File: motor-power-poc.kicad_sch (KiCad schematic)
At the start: 47 parts, among them J5 Conn_01x04_Pin, SW1 SW_Push, SW2 SW_Push, U1 QRE1113GR, U2 QRE1113GR, U3 QRE1113GR, U4 ESP32-S3FH4R2, Y1 48M

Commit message: schem: add ordering info to BOM
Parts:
- C2, C3, C4: Basic (none) -> Y; JLCPCB Part # (none) -> C307331; Manufacturer (none) -> Samsung Electro-Mechanics; Manufacturer Part Number (none) -> CL05B104KB54PNC
- R1, R2, R3: footprint Resistor_SMD:R_0402_1005Metric -> Resistor_SMD:R_0603_1608Metric; Basic (none) -> Y; JLCPCB Part # (none) -> C23212; Manufacturer (none) -> Uniroyal Elec; Manufacturer Part Number (none) -> 0603WAF6801T5E
- R4: Basic (none) -> Y; JLCPCB Part # (none) -> C23182; Manufacturer (none) -> Uniroyal Elec; Manufacturer Part Number (none) -> 0603WAF470JT5E
- R5: Basic (none) -> Y; JLCPCB Part # (none) -> C4275; Manufacturer (none) -> Uniroyal Elec; Manufacturer Part Number (none) -> 0603WAF750JT5E
- R6: Basic (none) -> Y; JLCPCB Part # (none) -> C22775; Manufacturer (none) -> Uniroyal Elec; Manufacturer Part Number (none) -> 0603WAF1000T5E
- TP1: Basic (none) -> X; JLCPCB Part # (none) -> C2906768; Manufacturer (none) -> Keystone; Manufacturer Part Number (none) -> 5015
- U1, U2, U3: Basic (none) -> X; JLCPCB Part # (none) -> C232862; Manufacturer (none) -> onsemi; Manufacturer Part Number (none) -> QRE1113GR

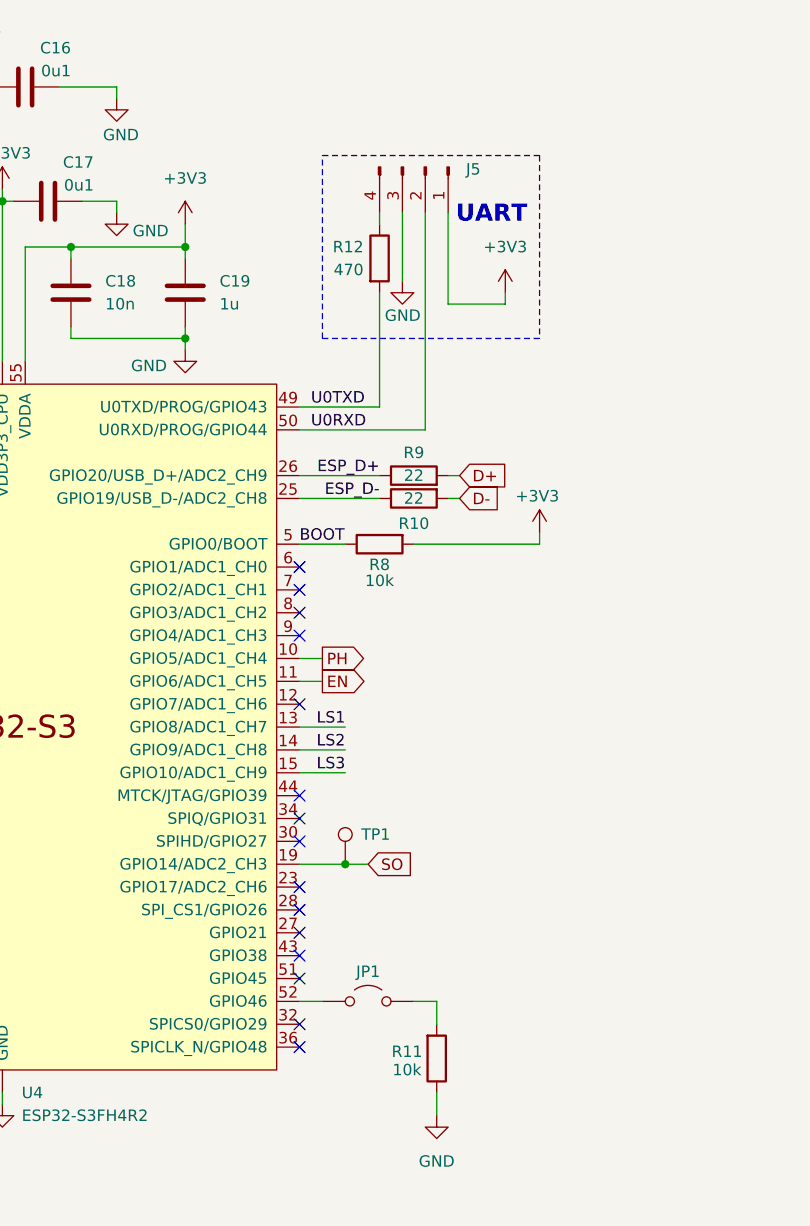
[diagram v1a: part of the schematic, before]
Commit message: schem: renumber
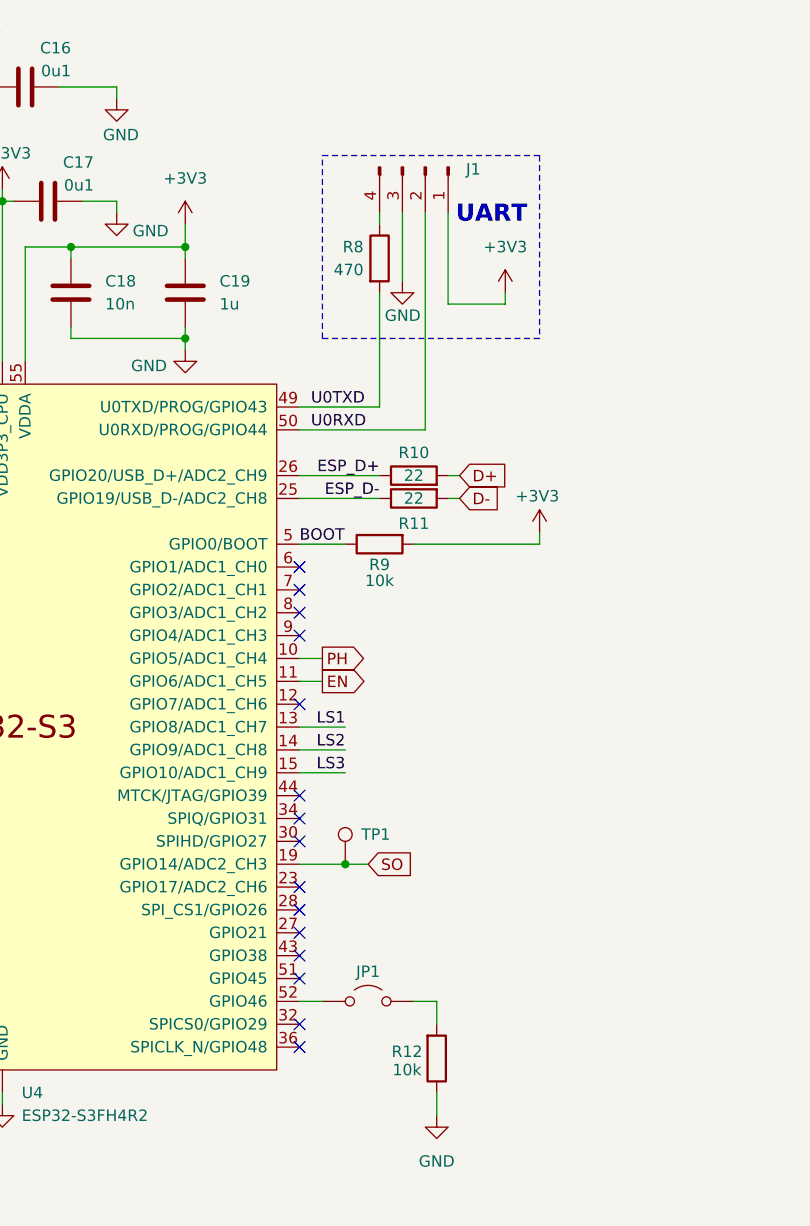
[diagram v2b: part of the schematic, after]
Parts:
- renumbered J5 to J1, R9 to R10, R10 to R11, R11 to R12, R12 to R8, R8 to R9
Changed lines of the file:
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@@
 		(on_board yes)
 		(dnp no)
-		(property "Reference" "R10"
+		(property "Reference" "R11"
 			(at 245.11 70.104 90)
 			(effects
@@
 			(project "motor-power-poc"
 				(path "/a1dc4c9e-7b20-4b66-a693-9133bc644c6b"
-					(reference "R10")
+					(reference "R11")
 					(unit 1)
 				)
@@
 		(on_board yes)
 		(dnp no)
-		(property "Reference" "J5"
+		(property "Reference" "J1"
 			(at 251.714 30.734 90)
 			(effects
@@
 			(project "motor-power-poc"
 				(path "/a1dc4c9e-7b20-4b66-a693-9133bc644c6b"
-					(reference "J5")
+					(reference "J1")
 					(unit 1)
 				)
@@
 		(dnp no)
 		(fields_autoplaced yes)
-		(property "Reference" "#PWR029"
+		(property "Reference" "#PWR030"
 			(at 247.65 142.24 0)
 			(effects
@@
 			(project "motor-power-poc"
 				(path "/a1dc4c9e-7b20-4b66-a693-9133bc644c6b"
-					(reference "#PWR029")
+					(reference "#PWR030")
 					(unit 1)
 				)
@@
 		(on_board yes)
 		(dnp no)
-		(property "Reference" "R9"
+		(property "Reference" "R10"
 			(at 245.11 62.23 90)
 			(effects
@@
 			(project "motor-power-poc"
 				(path "/a1dc4c9e-7b20-4b66-a693-9133bc644c6b"
-					(reference "R9")
+					(reference "R10")
 					(unit 1)
 				)
@@
 		(on_board yes)
 		(dnp no)
-		(property "Reference" "R11"
+		(property "Reference" "R12"
 			(at 244.348 128.778 0)
 			(effects
@@
 			(project "motor-power-poc"
 				(path "/a1dc4c9e-7b20-4b66-a693-9133bc644c6b"
-					(reference "R11")
+					(reference "R12")
 					(unit 1)
 				)
@@
 		(on_board yes)
 		(dnp no)
-		(property "Reference" "#PWR086"
+		(property "Reference" "#PWR029"
 			(at 243.84 49.53 0)
 			(effects
@@
 			(project "motor-power-poc"
 				(path "/a1dc4c9e-7b20-4b66-a693-9133bc644c6b"
-					(reference "#PWR086")
+					(reference "#PWR029")
 					(unit 1)
 				)
@@
 		(on_board yes)
 		(dnp no)
-		(property "Reference" "#PWR030"
+		(property "Reference" "#PWR032"
 			(at 259.08 74.93 0)
 			(effects
@@
 			(project "motor-power-poc"
 				(path "/a1dc4c9e-7b20-4b66-a693-9133bc644c6b"
-					(reference "#PWR030")
+					(reference "#PWR032")
 					(unit 1)
 				)
@@
 		(dnp no)
 		(fields_autoplaced yes)
-		(property "Reference" "#PWR087"
+		(property "Reference" "#PWR031"
 			(at 255.27 48.26 0)
 			(effects
@@
 			(project "motor-power-poc"
 				(path "/a1dc4c9e-7b20-4b66-a693-9133bc644c6b"
-					(reference "#PWR087")
+					(reference "#PWR031")
 					(unit 1)
 				)
@@
 		(on_board yes)
 		(dnp no)
-		(property "Reference" "R8"
+		(property "Reference" "R9"
 			(at 241.3 74.676 90)
 			(effects
@@
 			(project "motor-power-poc"
 				(path "/a1dc4c9e-7b20-4b66-a693-9133bc644c6b"
-					(reference "R8")
+					(reference "R9")
 					(unit 1)
 				)
@@
 		(on_board yes)
 		(dnp no)
-		(property "Reference" "R12"
+		(property "Reference" "R8"
 			(at 239.522 39.37 0)
 			(effects
@@
 			(project "motor-power-poc"
 				(path "/a1dc4c9e-7b20-4b66-a693-9133bc644c6b"
-					(reference "R12")
+					(reference "R8")
 					(unit 1)
 				)

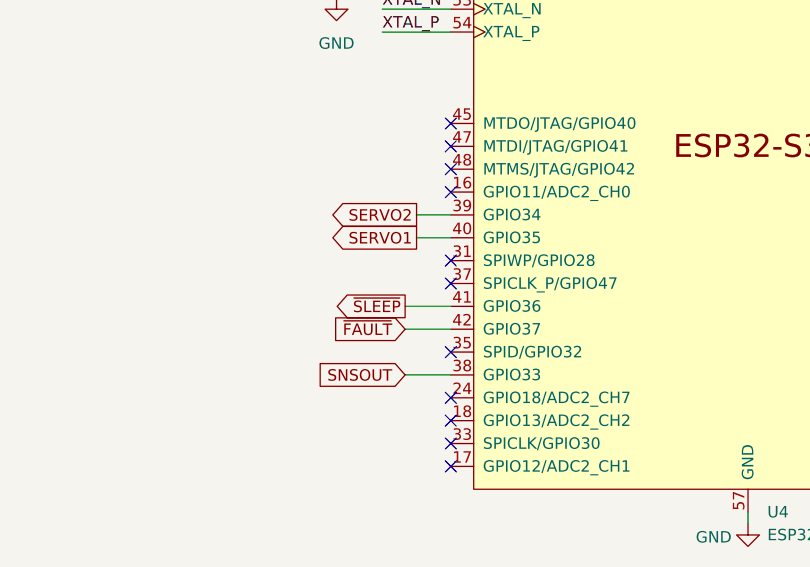
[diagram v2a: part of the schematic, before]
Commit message: schem: connect TPS2121 ST pin to MCU
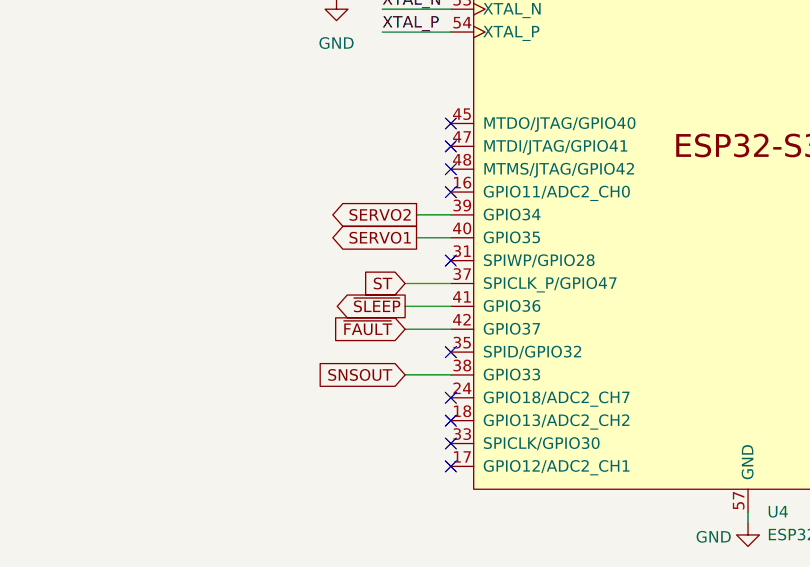
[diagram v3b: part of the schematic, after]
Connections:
- net ST: now reaches U4.37 (SPICLK_P/GPIO47)
- no-connect marks 28 -> 27
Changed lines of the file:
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@@
-	)
-	(no_connect
-		(at 166.37 107.95)
 	)
 	(no_connect
@@
 		(pts
 			(xy 162.56 100.33) (xy 166.37 100.33)
+		)
+		(stroke
+			(width 0)
+			(type default)
+		)
+	)
+	(wire
+		(pts
+			(xy 161.29 107.95) (xy 166.37 107.95)
 		)
 		(stroke
@@
 				(hide yes)
 			)
+		)
+	)
+	(global_label "ST"
+		(shape input)
+		(at 161.29 107.95 180)
+		(fields_autoplaced yes)
+		(effects
+			(font
+				(size 1.27 1.27)
+			)
+			(justify right)
+		)
+		(property "Intersheetrefs" "${INTERSHEET_REFS}"
+			(at 156.1277 107.95 0)
+			(effects
+				(font
+					(size 1.27 1.27)
+				)
+				(justify right)
+				(hide yes)
+			)

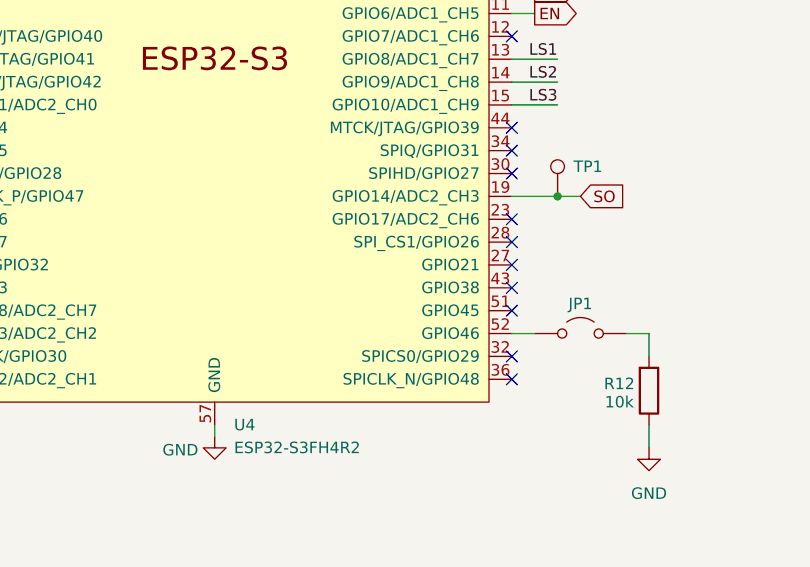
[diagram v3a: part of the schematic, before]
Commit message: pcb: add TPS5430 layout
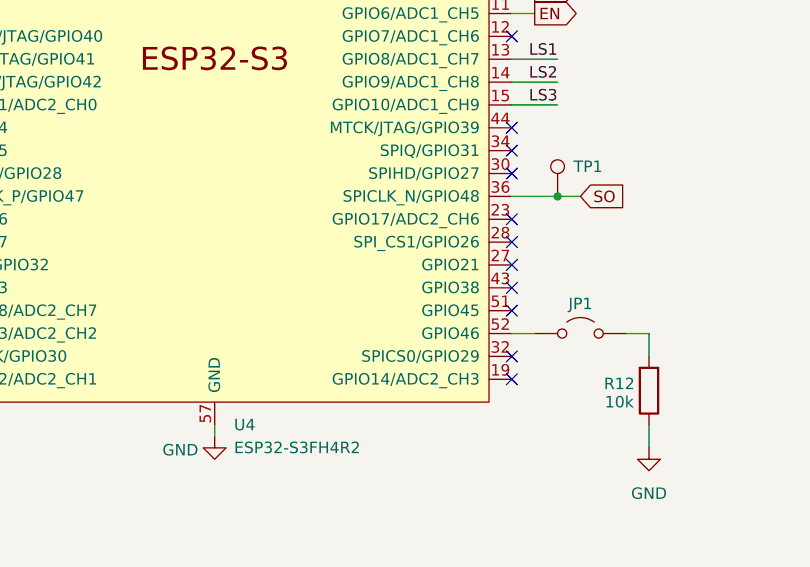
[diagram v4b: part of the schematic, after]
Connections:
- net SO: now also U4.36 (SPICLK_N/GPIO48); no longer U4.19 (GPIO14/ADC2_CH3)

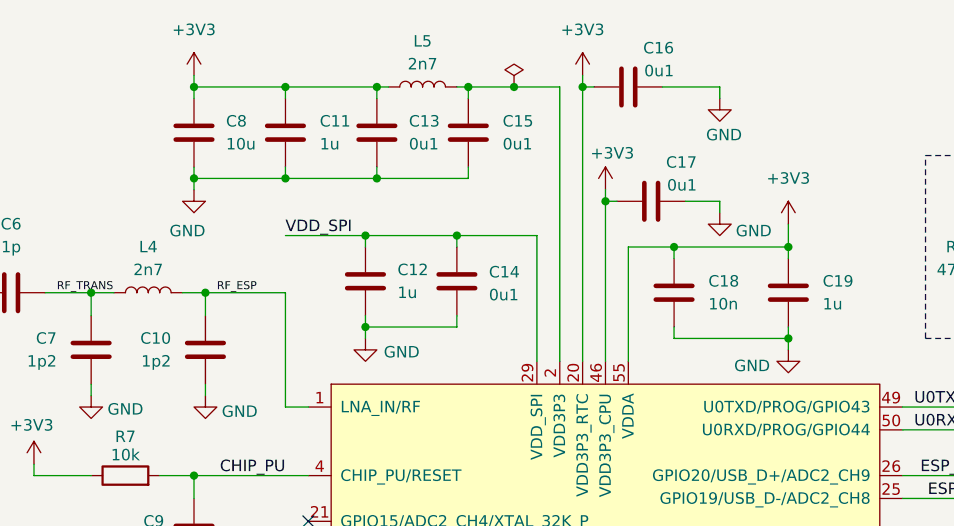
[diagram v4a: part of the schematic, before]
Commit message: schem: remove extra decoupling caps
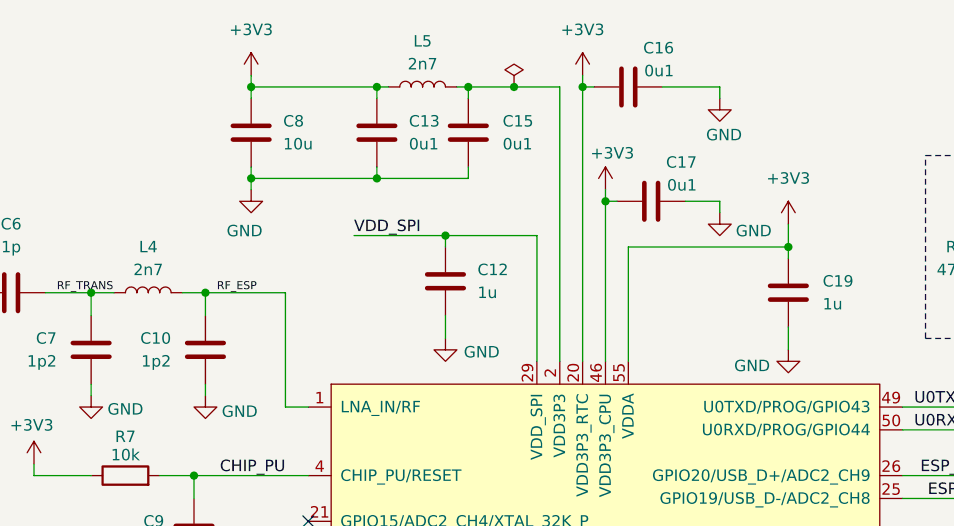
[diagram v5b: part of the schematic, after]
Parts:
- removed C11: 1u, Capacitor_SMD:C_0402_1005Metric, symbol Device:C
- removed C14: 0u1, Capacitor_SMD:C_0402_1005Metric, symbol Device:C
- removed C18: 10n, Capacitor_SMD:C_0402_1005Metric, symbol Device:C
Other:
- moved on the sheet: C12, C8

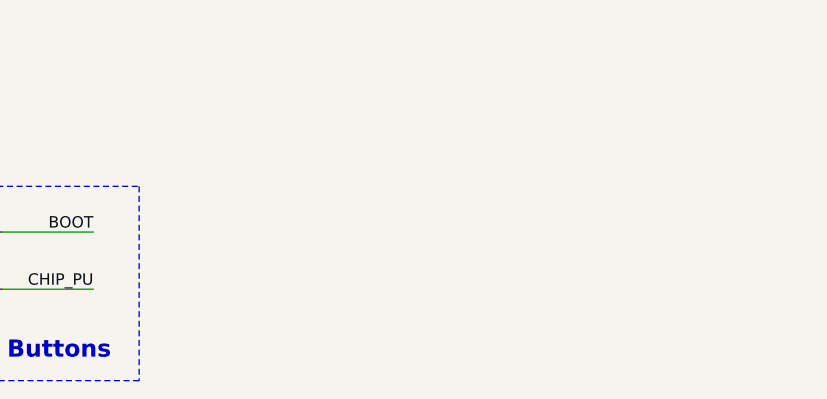
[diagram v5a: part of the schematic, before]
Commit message: schem: add fiduals, tooling and mounting holes
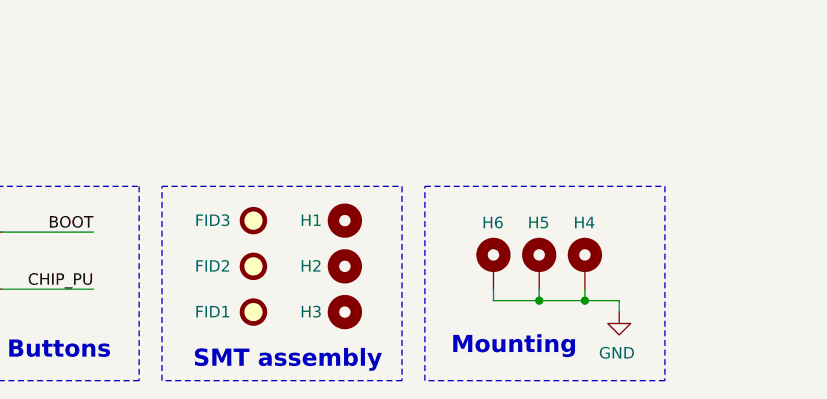
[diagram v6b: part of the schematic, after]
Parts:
- added FID1, FID2, FID3: Fiducial, Fiducial:Fiducial_1mm_Mask2mm, symbol Mechanical:Fiducial
- added H1, H2, H3: MountingHole, MountingHole:ToolingHole_1.152mm, symbol Mechanical:MountingHole
- added H4, H5, H6: MountingHole_Pad, MountingHole:MountingHole_2.2mm_M2_Pad_Via, symbol Mechanical:MountingHole_Pad
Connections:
- net GND: now also H4.1, H5.1, H6.1
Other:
- note added: "Mounting"
- note added: "SMT assembly"

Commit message: schem: use espressif QFN-56 footprint for ESP32S3 MCU
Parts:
- U4: footprint Package_DFN_QFN:QFN-56-1EP_7x7mm_P0.4mm_EP5.6x5.6mm -> Package_DFN_QFN:QFN-56-1EP_7x7mm_P0.4mm_EP4x4mm_ThermalVias
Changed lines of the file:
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@@
 			)
 		)
-		(property "Footprint" "Package_DFN_QFN:QFN-56-1EP_7x7mm_P0.4mm_EP5.6x5.6mm"
+		(property "Footprint" "Package_DFN_QFN:QFN-56-1EP_7x7mm_P0.4mm_EP4x4mm_ThermalVias"
 			(at 199.39 140.97 0)
 			(effects
